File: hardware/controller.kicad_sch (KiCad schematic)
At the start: 38 parts, among them J1 Connector, USB-TYPE-C-16P, J2 AXK6F20347YG, J3 AFA01-S08FCA-00, U1 ESP32-C6-WROOM-1, U2 BQ24074RGTR, U3 TLA2518IRTER, U6 TPS62142RGTR

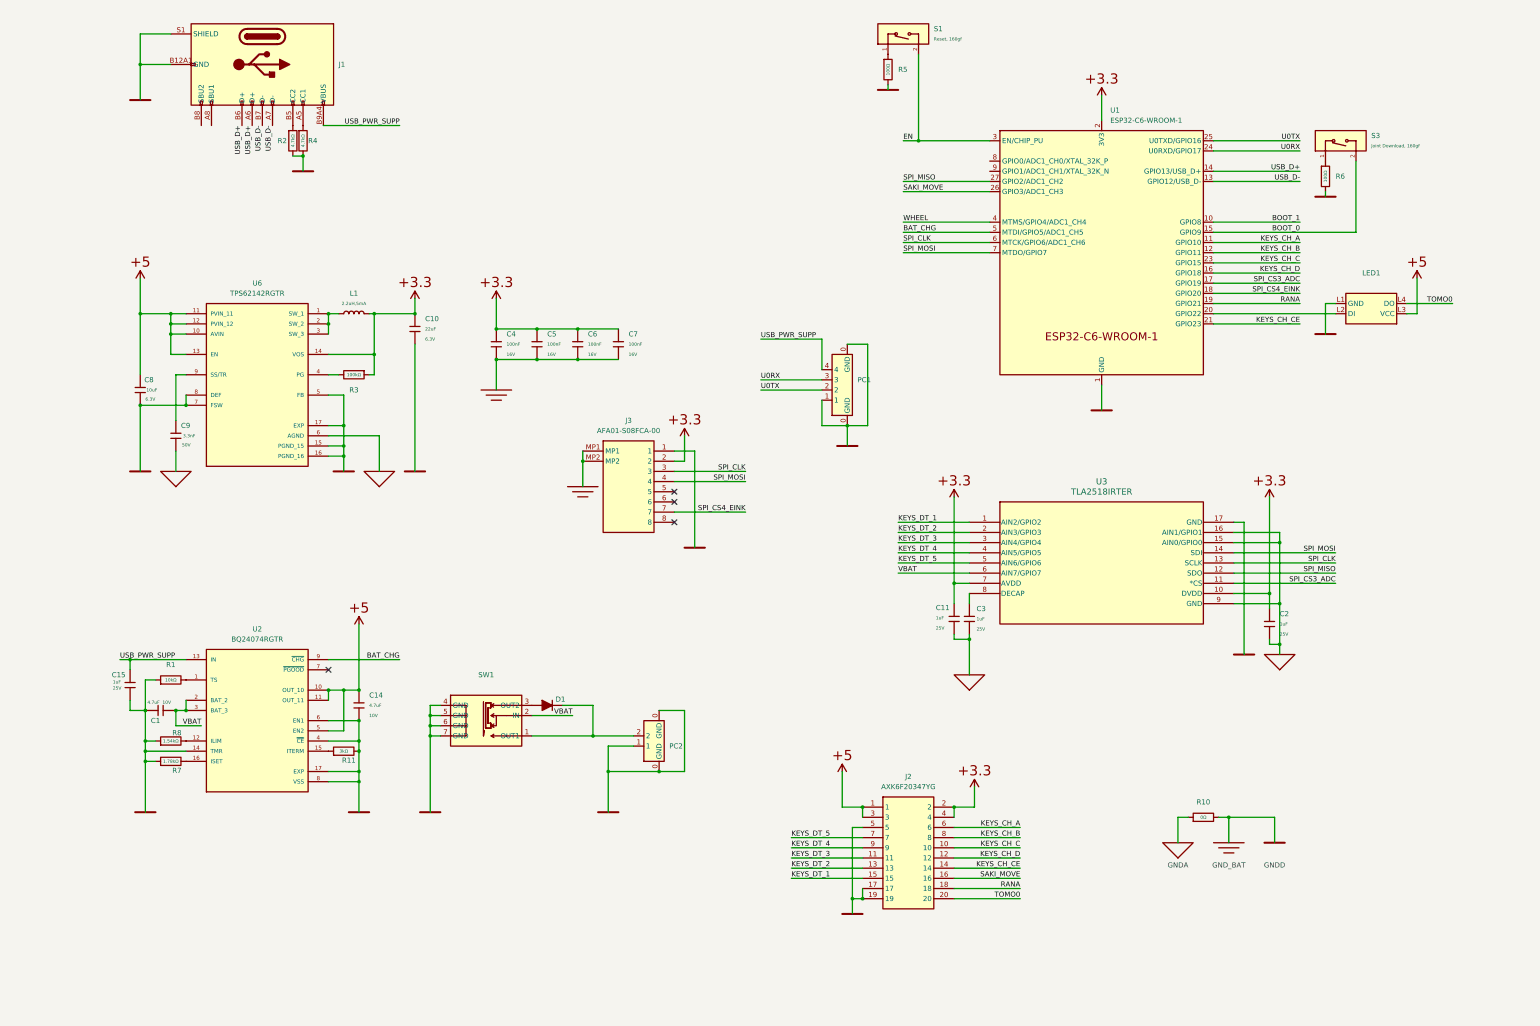
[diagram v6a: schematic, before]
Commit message: :sparkles: use side reset button
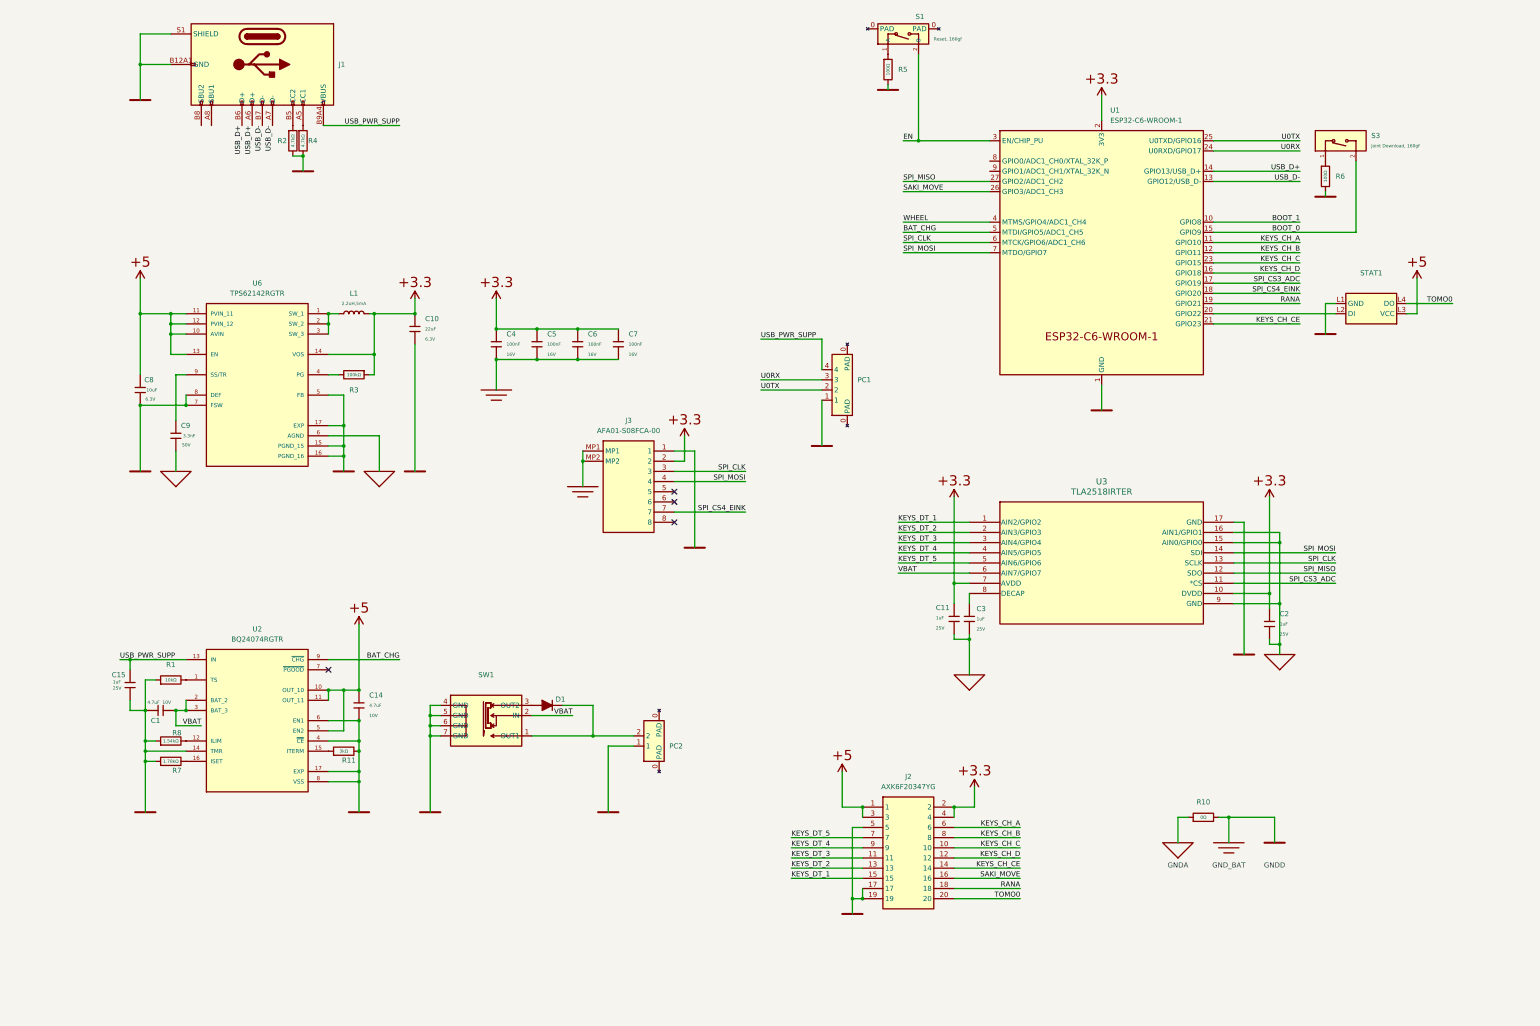
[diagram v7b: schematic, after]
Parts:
- S1: footprint KeysDock:SW_TS-1088-AR02016 -> KeysDock:TS24CA; symbol components:Tactile Button, 160gf, 12V, 50mA, 4.0mm -> components:TS24CA
- renumbered LED1 to STAT1
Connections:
- net P,E: no longer PC1.0 (GND), PC2.0 (GND)
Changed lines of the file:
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@@
 	)
 	(junction
-		(at 181.61 213.36)
-		(diameter 0)
-		(color 0 0 0 0)
-	)
-	(junction
 		(at 102.87 132.08)
 		(diameter 0)
@@
 	)
 	(junction
-		(at 228.6 127)
-		(diameter 0)
-		(color 0 0 0 0)
-	)
-	(junction
 		(at 53.34 208.28)
 		(diameter 0)
@@
 	)
 	(junction
-		(at 168.91 213.36)
-		(diameter 0)
-		(color 0 0 0 0)
-	)
-	(junction
 		(at 165.1 204.47)
 		(diameter 0)
@@
 	(wire
 		(pts
-			(xy 168.91 213.36) (xy 181.61 213.36)
-		)
-		(stroke
-			(width 0)
-			(type default)
-		)
-	)
-	(wire
-		(pts
 			(xy 157.48 196.85) (xy 165.1 196.85)
 		)
@@
 	(wire
 		(pts
-			(xy 222.25 120.65) (xy 222.25 127)
-		)
-		(stroke
-			(width 0)
-			(type default)
-		)
-	)
-	(wire
-		(pts
 			(xy 259.08 180.34) (xy 259.08 179.07)
 		)
@@
 	(wire
 		(pts
-			(xy 187.96 198.12) (xy 187.96 213.36)
-		)
-		(stroke
-			(width 0)
-			(type default)
-		)
-	)
-	(wire
-		(pts
 			(xy 335.28 224.79) (xy 335.28 231.14)
 		)
@@
 	(wire
 		(pts
-			(xy 181.61 213.36) (xy 187.96 213.36)
-		)
-		(stroke
-			(width 0)
-			(type default)
-		)
-	)
-	(wire
-		(pts
 			(xy 320.04 66.04) (xy 341.63 66.04)
 		)
@@
 	(wire
 		(pts
-			(xy 222.25 127) (xy 228.6 127)
-		)
-		(stroke
-			(width 0)
-			(type default)
-		)
-	)
-	(wire
-		(pts
 			(xy 320.04 58.42) (xy 341.63 58.42)
 		)
@@
 	(wire
 		(pts
-			(xy 168.91 207.01) (xy 168.91 213.36)
-		)
-		(stroke
-			(width 0)
-			(type default)
-		)
-	)
-	(wire
-		(pts
-			(xy 181.61 198.12) (xy 187.96 198.12)
+			(xy 168.91 207.01) (xy 168.91 223.52)
 		)
 		(stroke
@@
 	(wire
 		(pts
-			(xy 233.68 106.68) (xy 233.68 127)
-		)
-		(stroke
-			(width 0)
-			(type default)
-		)
-	)
-	(wire
-		(pts
 			(xy 325.12 156.21) (xy 336.55 156.21)
 		)
@@
 	(wire
 		(pts
-			(xy 355.6 60.96) (xy 355.6 78.74)
-		)
-		(stroke
-			(width 0)
-			(type default)
-		)
-	)
-	(wire
-		(pts
-			(xy 228.6 106.68) (xy 233.68 106.68)
+			(xy 222.25 120.65) (xy 222.25 132.08)
 		)
 		(stroke
@@
 	(wire
 		(pts
-			(xy 233.68 127) (xy 228.6 127)
+			(xy 355.6 60.96) (xy 355.6 78.74)
 		)
 		(stroke
@@
 	(wire
 		(pts
-			(xy 228.6 132.08) (xy 228.6 127)
-		)
-		(stroke
-			(width 0)
-			(type default)
-		)
-	)
-	(wire
-		(pts
 			(xy 347.98 96.52) (xy 347.98 104.14)
 		)
@@
 	(wire
 		(pts
-			(xy 168.91 213.36) (xy 168.91 223.52)
-		)
-		(stroke
-			(width 0)
-			(type default)
-		)
-	)
-	(wire
-		(pts
 			(xy 271.78 229.87) (xy 255.27 229.87)
 		)
@@
 		(dnp no)
 		(fields_autoplaced yes)
-		(property "Reference" "LED1"
+		(property "Reference" "STAT1"
 			(at 359.41 88.9 0)
 			(effects
@@
 			(project ""
 				(path "/a4e7072d-1db6-48c9-937c-096c1ce61d37"
-					(reference "LED1")
+					(reference "STAT1")
 					(unit 1)
 				)
@@
 	)
 	(symbol
-		(lib_id "components:Tactile Button, 160gf, 12V, 50mA, 4.0mm")
-		(at 241.3 29.21 90)
+		(lib_id "components:TS24CA")
+		(at 242.57 29.21 90)
 		(unit 1)
 		(exclude_from_sim no)
@@
 		(on_board yes)
 		(dnp no)
-		(fields_autoplaced yes)
 		(property "Reference" "S1"
-			(at 250.19 27.9399 90)
+			(at 245.618 24.892 90)
 			(effects
 				(font
@@
 			)
 		)
-		(property "Footprint" "KeysDock:SW_TS-1088-AR02016"
-			(at 251.46 29.21 0)
+		(property "Footprint" "KeysDock:TS24CA"
+			(at 242.57 29.21 0)
 			(effects
 				(font
 					(size 1.27 1.27)
-					(italic yes)
 				)
 				(hide yes)
@@
 		)
 		(property "Datasheet" "${KIPRJMOD}/docs/C720477.pdf"
-			(at 241.173 31.496 0)
+			(at 242.57 29.21 0)
 			(effects
 				(font
 					(size 1.27 1.27)
 				)
-				(justify left)
 				(hide yes)
 			)
 		)
 		(property "Description" "Without 50mA 4mm 100MΩ 100000 Times 12V 160gf 3mm 2mm Round Button Standing paste SPST SMD Tactile Switches ROHS"
-			(at 241.3 29.21 0)
+			(at 242.57 29.21 0)
 			(effects
 				(font
@@
 		)
 		(property "LCSC" "C720477"
-			(at 241.3 29.21 0)
+			(at 242.57 29.21 0)
 			(effects
 				(font
@@
 		)
 		(property "Stock" "346801"
-			(at 241.3 29.21 0)
+			(at 242.57 29.21 0)
 			(effects
 				(font
@@
 		)
 		(property "Price" "0.044USD"
-			(at 241.3 29.21 0)
+			(at 242.57 29.21 0)
 			(effects
 				(font
@@
 		)
 		(property "Process" "SMT"
-			(at 241.3 29.21 0)
+			(at 242.57 29.21 0)
 			(effects
 				(font
@@
 		)
 		(property "Minimum Qty" "5"
-			(at 241.3 29.21 0)
+			(at 242.57 29.21 0)
 			(effects
 				(font
@@
 		)
 		(property "Attrition Qty" "4"
-			(at 241.3 29.21 0)
+			(at 242.57 29.21 0)
 			(effects
 				(font
@@
 		)
 		(property "Class" "Basic Component"
-			(at 241.3 29.21 0)
+			(at 242.57 29.21 0)
 			(effects
 				(font
@@
 		)
 		(property "Category" "Switches,Tactile Switches"
-			(at 241.3 29.21 0)
+			(at 242.57 29.21 0)
 			(effects
 				(font
@@
 		)
 		(property "Manufacturer" "XUNPU"
-			(at 241.3 29.21 0)
+			(at 242.57 29.21 0)
 			(effects
 				(font
@@
 		)
 		(property "Part" "TS-1088-AR02016"
-			(at 241.3 29.21 0)
+			(at 242.57 29.21 0)
 			(effects
 				(font
@@
 		)
 		(property "Switch Length" "4mm"
-			(at 241.3 29.21 0)
+			(at 242.57 29.21 0)
 			(effects
 				(font
@@
 		)
 		(property "Voltage Rating (Dc)" "12V"
-			(at 241.3 29.21 0)
+			(at 242.57 29.21 0)
 			(effects
 				(font
@@
 		)
 		(property "With Lamp" "No"
-			(at 241.3 29.21 0)
+			(at 242.57 29.21 0)
 			(effects
 				(font
@@
 		)
 		(property "Operating Force" "160gf@±50gf"
-			(at 241.3 29.21 0)
+			(at 242.57 29.21 0)
 			(effects
 				(font
@@
 		)
 		(property "Actuator/Cap Color" "Black"
-			(at 241.3 29.21 0)
+			(at 242.57 29.21 0)
 			(effects
 				(font
@@
 		)
 		(property "Mechanical Life" "100000 Times"
-			(at 241.3 29.21 0)
+			(at 242.57 29.21 0)
 			(effects
 				(font
@@
 		)
 		(property "Strike Gundam" "NO"
-			(at 241.3 29.21 0)
+			(at 242.57 29.21 0)
 			(effects
 				(font
@@
 		)
 		(property "Circuit" "SPST"
-			(at 241.3 29.21 0)
+			(at 242.57 29.21 0)
 			(effects
 				(font
@@
 		)
 		(property "Switch Height" "2mm"
-			(at 241.3 29.21 0)
+			(at 242.57 29.21 0)
 			(effects
 				(font
@@
 		)
 		(property "Actuator Style" "Round Button"
-			(at 241.3 29.21 0)
+			(at 242.57 29.21 0)
 			(effects
 				(font
@@
 		)
 		(property "Switch Width" "3mm"
-			(at 241.3 29.21 0)
+			(at 242.57 29.21 0)
 			(effects
 				(font
@@
 		)
 		(property "Contact Current" "50mA"
-			(at 241.3 29.21 0)
+			(at 242.57 29.21 0)
 			(effects
 				(font
@@
 		)
 		(property "Operating Temperature" "-30°C~+80°C"
-			(at 241.3 29.21 0)
+			(at 242.57 29.21 0)
 			(effects
 				(font
@@
 		)
 		(property "Mounting Style" "Brick nogging"
-			(at 241.3 29.21 0)
+			(at 242.57 29.21 0)
 			(effects
 				(font
@@
 		)
 		(property "Insulation Resistance" "100MΩ"
-			(at 241.3 29.21 0)
+			(at 242.57 29.21 0)
 			(effects
 				(font
@@
 		)
 		(property "Pin Style" "SMDSplicing"
-			(at 241.3 29.21 0)
+			(at 242.57 29.21 0)
 			(effects
 				(font
@@
 		(pin "1"
 		)
+		(pin "0"
+		)
+		(pin "0"
+		)
 		(instances
 			(project "controller"
@@
 	(symbol
 		(lib_id "PCM_Generic:P,0")
-		(at 228.6 132.08 0)
+		(at 222.25 132.08 0)
 		(unit 1)
 		(exclude_from_sim no)
@@
 		(fields_autoplaced yes)
 		(property "Reference" "#PWR011"
-			(at 232.41 128.27 0)
+			(at 226.06 128.27 0)
 			(effects
 				(font
@@
 		)
 		(property "Value" "P,E"
-			(at 232.41 132.08 0)
+			(at 226.06 132.08 0)
 			(effects
 				(font
@@
 		)
 		(property "Footprint" ""
-			(at 228.6 132.08 0)
+			(at 222.25 132.08 0)
 			(effects
 				(font
@@
 		)
 		(property "Datasheet" ""
-			(at 228.6 132.08 0)
+			(at 222.25 132.08 0)
 			(effects
 				(font
@@
 		)
 		(property "Description" "global node 0; simplified functional (equipotential) bonding (FB); simplified frame/chassis"
-			(at 228.6 132.08 0)
+			(at 222.25 132.08 0)
 			(effects
 				(font

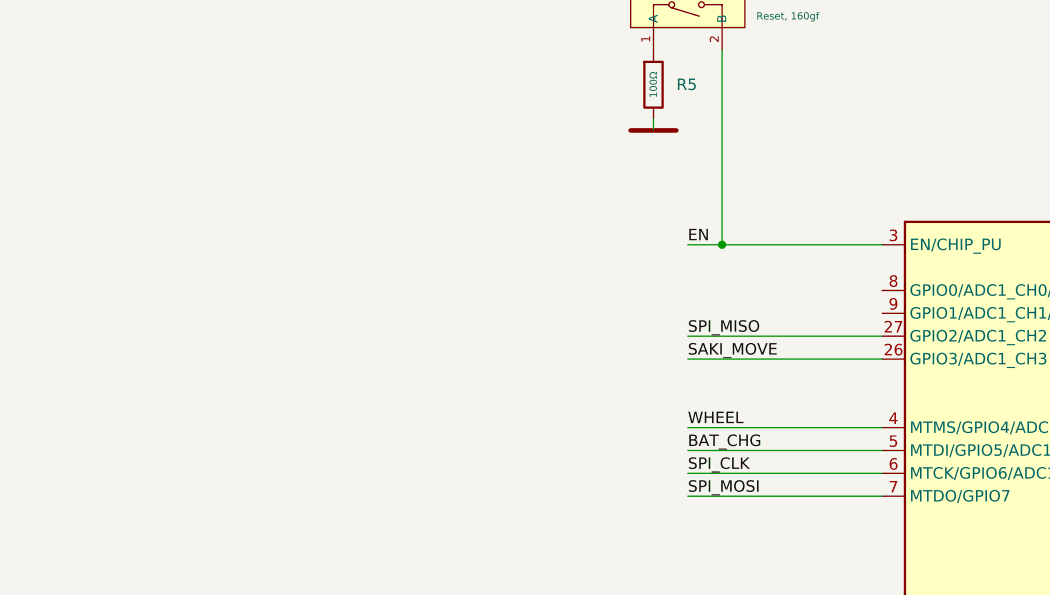
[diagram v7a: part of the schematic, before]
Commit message: :sparkles: finish all hardware designs except external
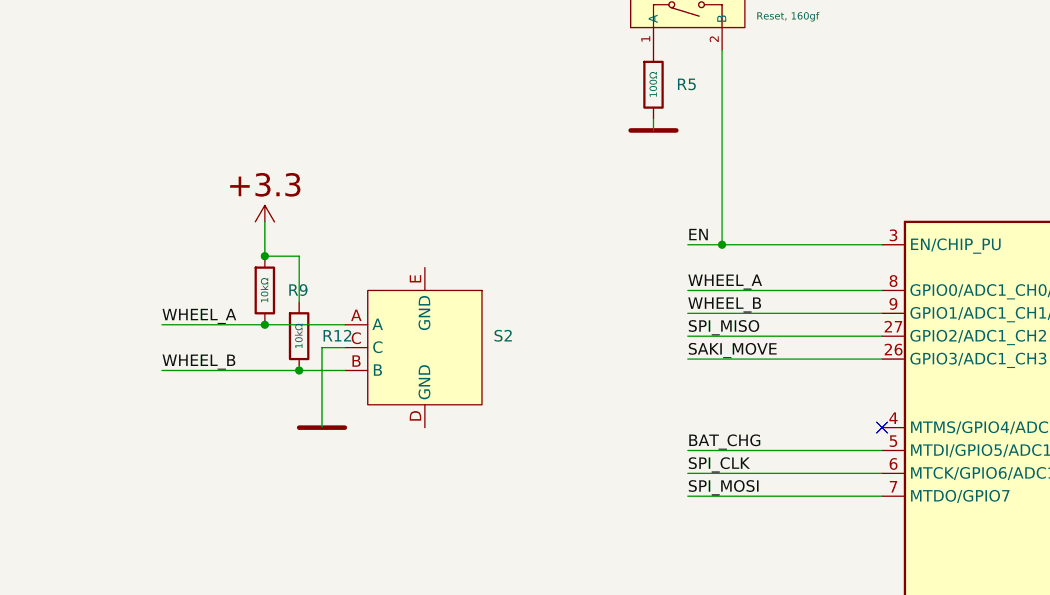
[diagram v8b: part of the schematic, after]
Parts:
- added R12, R9: 10kΩ, KeysDock:R_0402, symbol components:0402,10kΩ
- added S2: ~, KeysDock:EC12E1240301, symbol components:EC12E1240301
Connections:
- net P,+3.3: now also R12.1, R9.1
- net P,E: now also S2.C
- net WHEEL_A: now reaches U1.8 (GPIO0/ADC1_CH0/XTAL_32K_P)
- net WHEEL_A: now also R9.2, S2.A
- net WHEEL_B: now reaches U1.9 (GPIO1/ADC1_CH1/XTAL_32K_N)
- net WHEEL_B: now also R12.2, S2.B
- net WHEEL: no longer names the net of U1.4 (MTMS/GPIO4/ADC1_CH4)
- no-connect marks 4 -> 5
